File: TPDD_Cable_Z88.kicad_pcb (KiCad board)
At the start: 2 copper layers, 10.6 x 12.7 mm, 5 parts, among them J1 Wire Solder Pads, J2 TPDD, Q1 DTA114EKA, Q2 DTA114EKA, Q3 DTA114EKA

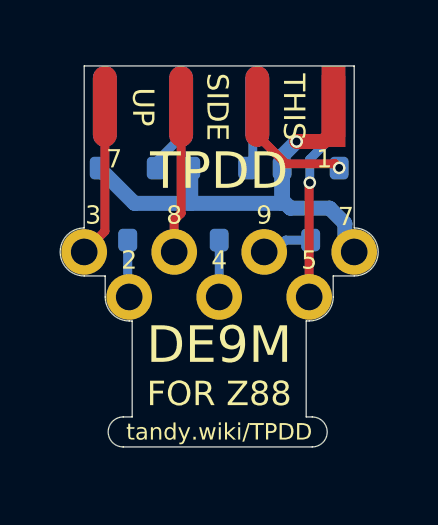
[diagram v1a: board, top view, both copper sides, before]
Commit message: bigger 2x4 solder pads, smaller wire holes
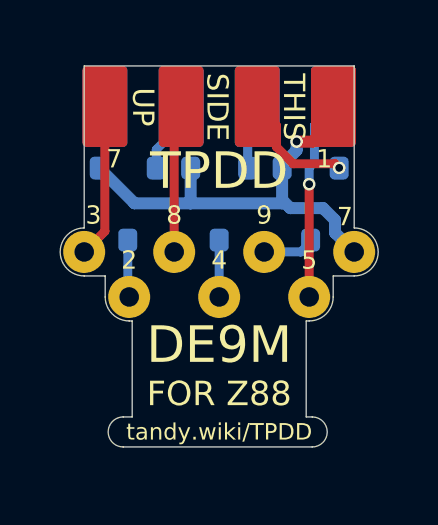
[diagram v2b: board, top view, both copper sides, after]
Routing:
- net /SG: track 16.8 -> 15.4 mm

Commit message: adjust board outline
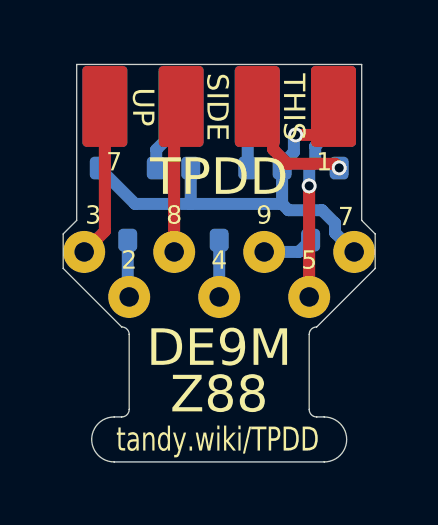
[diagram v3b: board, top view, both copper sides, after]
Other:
- board size 10.6 x 12.7 mm -> 10.4 x 13.2 mm
- net class Default: clearance 0.16 -> 0.2; trace_width 0.16 -> 0.2; via_dia 0.42 -> 0.5; via_drill 0.26 -> 0.3
- rule trace_clearance: 0.16 -> 0.2
- rule trace_min: 0.16 -> 0.2
- rule via_min_drill: 0.26 -> 0.3
- rule via_min_size: 0.42 -> 0.5
- board text added: "Q* DTA114EKA"
- board text added: "Z88"
- board text removed: "FOR Z88"
- board text removed: "Q*: DTA114EKA"
